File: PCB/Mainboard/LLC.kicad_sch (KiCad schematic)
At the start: 3 parts, among them U4 TXS0108EPW

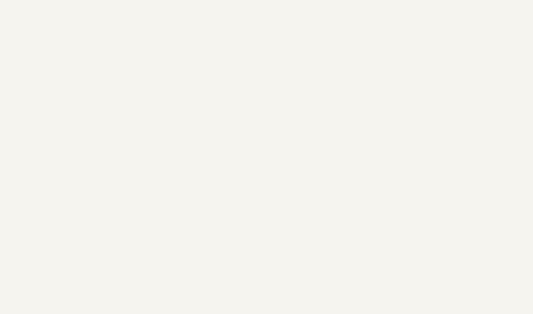
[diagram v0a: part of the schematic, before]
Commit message: Added setup, read and get Command
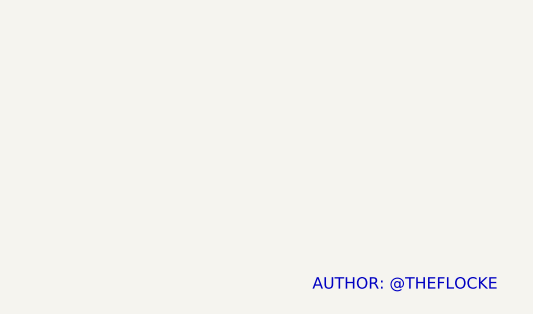
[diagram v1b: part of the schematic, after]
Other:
- note added: "AUTHOR: @THEFLOCKE"
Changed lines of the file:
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@@
 	(generator_version "9.0")
 	(paper "A4")
+	(text "AUTHOR: @THEFLOCKE"
+		(exclude_from_sim no)
+		(at 249.936 196.596 0)
+		(effects
+			(font
+				(face "KiCad Font")
+				(size 1.27 1.27)
+				(color 194 0 194 1)
+			)
+		)
+	)
 	(text "Nicht läner als 16.7ns"
 		(exclude_from_sim no)
